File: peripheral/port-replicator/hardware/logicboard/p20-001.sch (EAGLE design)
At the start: 27 parts, among them IC1 74ALS04N, J0 DC9V, J11 AUDIO_JACK_3.5MM_PTH, J12 AUDIO_JACK_3.5MM_PTH, J13 AUDIO_JACK_3.5MM_PTH, J14 AUDIO_JACK_3.5MM_PTH, J7 DIN5, J8 DIN5, J9 DIN5, X0 MKDSN1,5/2-5,08

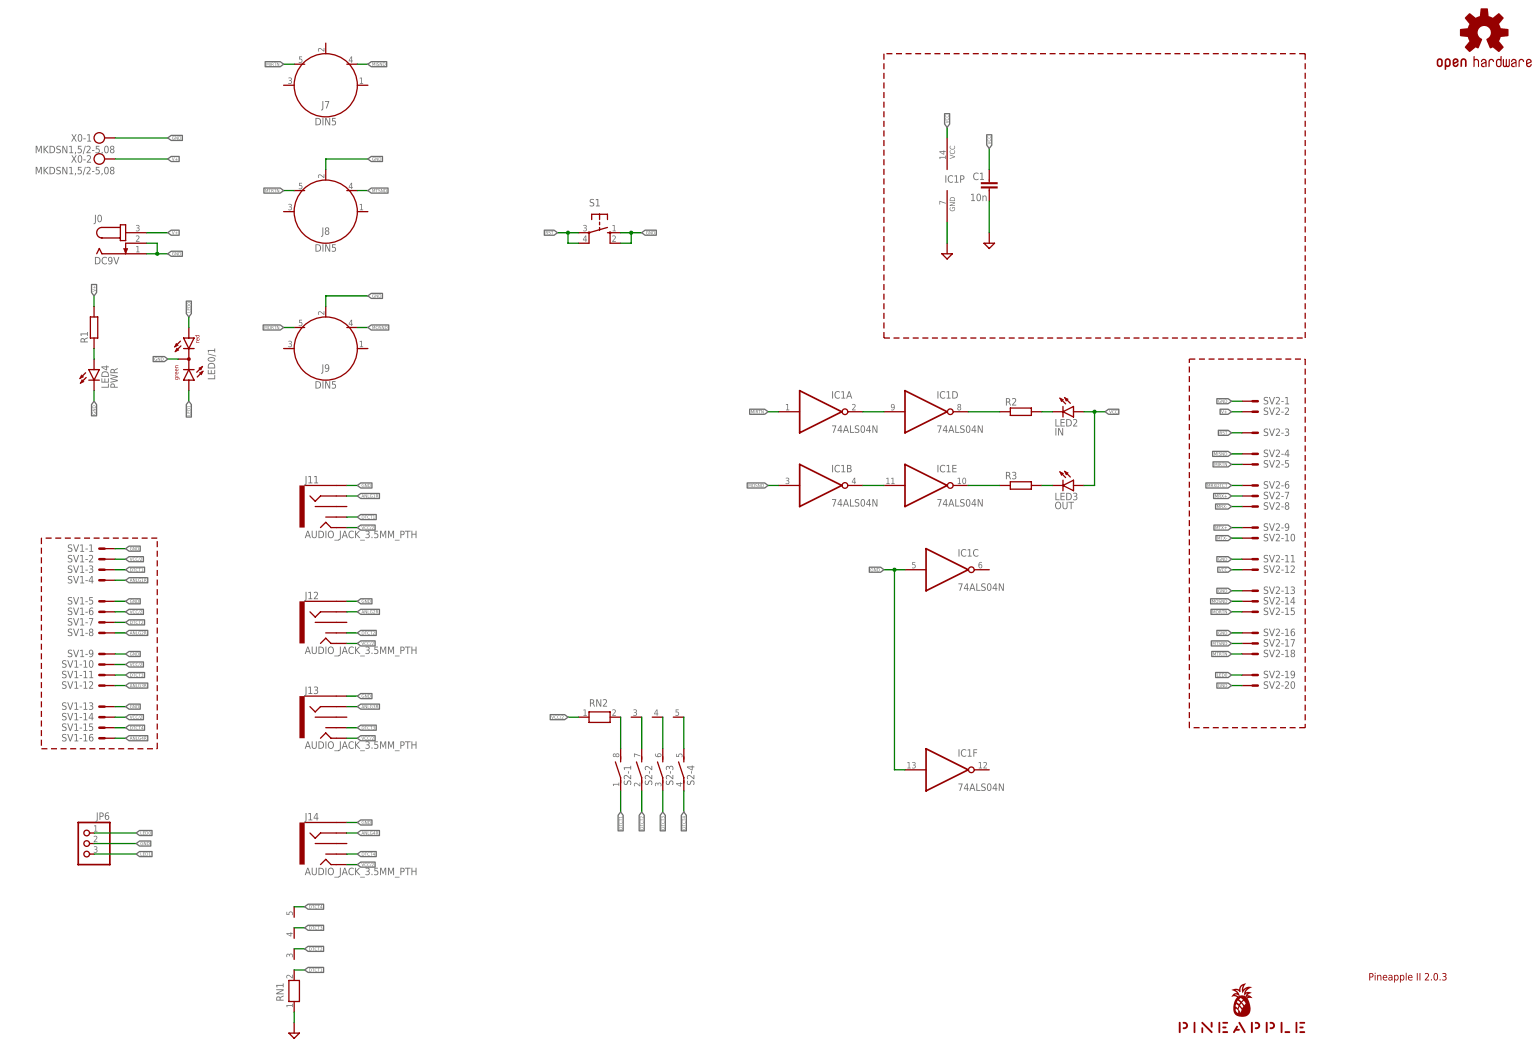
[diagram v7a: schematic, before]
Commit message: Renumbered parts of Pineapple II and port rep.
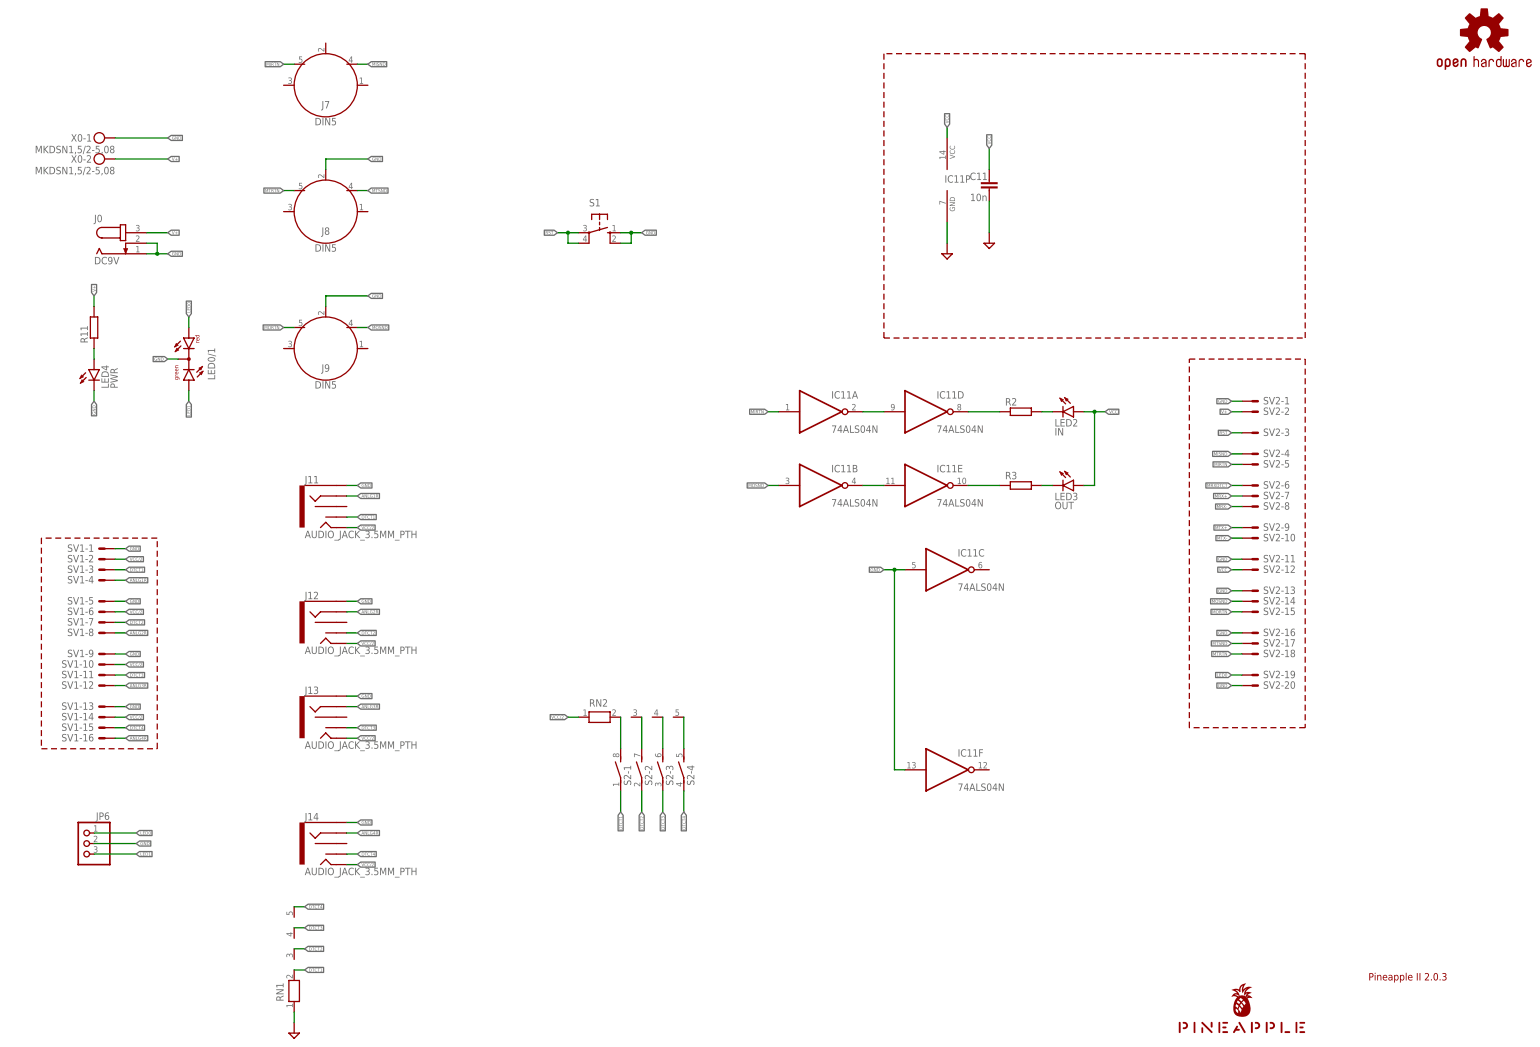
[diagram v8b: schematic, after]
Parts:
- renumbered C1 to C11, IC1 to IC11, R1 to R11
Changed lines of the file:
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@@
 <part name="SV2" library="con-ml" library_urn="urn:adsk.eagle:library:164" deviceset="ML20LE" device="" package3d_urn="urn:adsk.eagle:package:8685/1"/>
 <part name="SUPPLY26" library="supply2" deviceset="GND" device=""/>
-<part name="C1" library="resistor" library_urn="urn:adsk.eagle:library:348" deviceset="C-EU" device="025-024X044" package3d_urn="urn:adsk.eagle:package:23630/1" value="10n"/>
+<part name="C11" library="resistor" library_urn="urn:adsk.eagle:library:348" deviceset="C-EU" device="025-024X044" package3d_urn="urn:adsk.eagle:package:23630/1" value="10n"/>
 <part name="SV1" library="con-ml" library_urn="urn:adsk.eagle:library:164" deviceset="ML16LE" device="" package3d_urn="urn:adsk.eagle:package:8682/1"/>
 <part name="J7" library="SparkFun-Connectors" library_urn="urn:adsk.eagle:library:513" deviceset="DIN5" device="" package3d_urn="urn:adsk.eagle:package:38294/1"/>
@@
 <part name="J13" library="SparkFun-Connectors" library_urn="urn:adsk.eagle:library:513" deviceset="AUDIO_JACK_3.5MM" device="_PTH" package3d_urn="urn:adsk.eagle:package:37997/1"/>
 <part name="J14" library="SparkFun-Connectors" library_urn="urn:adsk.eagle:library:513" deviceset="AUDIO_JACK_3.5MM" device="_PTH" package3d_urn="urn:adsk.eagle:package:37997/1"/>
-<part name="IC1" library="74xx-us" library_urn="urn:adsk.eagle:library:88" deviceset="74*04" device="N" package3d_urn="urn:adsk.eagle:package:16407/2" technology="ALS" value="74ALS04N"/>
-<part name="R1" library="rcl" library_urn="urn:adsk.eagle:library:334" deviceset="R-EU_" device="0204/5" package3d_urn="urn:adsk.eagle:package:23488/1"/>
+<part name="IC11" library="74xx-us" library_urn="urn:adsk.eagle:library:88" deviceset="74*04" device="N" package3d_urn="urn:adsk.eagle:package:16407/2" technology="ALS" value="74ALS04N"/>
+<part name="R11" library="rcl" library_urn="urn:adsk.eagle:library:334" deviceset="R-EU_" device="0204/5" package3d_urn="urn:adsk.eagle:package:23488/1"/>
 <part name="R2" library="rcl" library_urn="urn:adsk.eagle:library:334" deviceset="R-EU_" device="0204/5" package3d_urn="urn:adsk.eagle:package:23488/1"/>
 <part name="LED4" library="led" library_urn="urn:adsk.eagle:library:259" deviceset="LED" device="3MM" package3d_urn="urn:adsk.eagle:package:15797/1" value="PWR"/>
@@
 </instance>
 <instance part="SUPPLY26" gate="GND" x="251.46" y="198.12" smashed="yes"/>
-<instance part="C1" gate="G$1" x="251.46" y="213.36" smashed="yes">
+<instance part="C11" gate="G$1" x="251.46" y="213.36" smashed="yes">
 <attribute name="NAME" x="248.92" y="213.36" size="1.778" layer="95" align="bottom-center"/>
 <attribute name="VALUE" x="248.92" y="208.28" size="1.778" layer="96" align="bottom-center"/>
@@
 <attribute name="VALUE" x="86.36" y="45.72" size="1.778" layer="96" font="vector"/>
 </instance>
-<instance part="IC1" gate="A" x="210.82" y="157.48" smashed="yes">
+<instance part="IC11" gate="A" x="210.82" y="157.48" smashed="yes">
 <attribute name="NAME" x="213.36" y="160.655" size="1.778" layer="95"/>
 <attribute name="VALUE" x="213.36" y="152.4" size="1.778" layer="96"/>
 </instance>
-<instance part="IC1" gate="B" x="210.82" y="139.7" smashed="yes">
+<instance part="IC11" gate="B" x="210.82" y="139.7" smashed="yes">
 <attribute name="NAME" x="213.36" y="142.875" size="1.778" layer="95"/>
 <attribute name="VALUE" x="213.36" y="134.62" size="1.778" layer="96"/>
 </instance>
-<instance part="IC1" gate="C" x="241.3" y="119.38" smashed="yes">
+<instance part="IC11" gate="C" x="241.3" y="119.38" smashed="yes">
 <attribute name="NAME" x="243.84" y="122.555" size="1.778" layer="95"/>
 <attribute name="VALUE" x="243.84" y="114.3" size="1.778" layer="96"/>
 </instance>
-<instance part="IC1" gate="D" x="236.22" y="157.48" smashed="yes">
+<instance part="IC11" gate="D" x="236.22" y="157.48" smashed="yes">
 <attribute name="NAME" x="238.76" y="160.655" size="1.778" layer="95"/>
 <attribute name="VALUE" x="238.76" y="152.4" size="1.778" layer="96"/>
 </instance>
-<instance part="IC1" gate="E" x="236.22" y="139.7" smashed="yes">
+<instance part="IC11" gate="E" x="236.22" y="139.7" smashed="yes">
 <attribute name="NAME" x="238.76" y="142.875" size="1.778" layer="95"/>
 <attribute name="VALUE" x="238.76" y="134.62" size="1.778" layer="96"/>
 </instance>
-<instance part="IC1" gate="F" x="241.3" y="71.12" smashed="yes">
+<instance part="IC11" gate="F" x="241.3" y="71.12" smashed="yes">
 <attribute name="NAME" x="243.84" y="74.295" size="1.778" layer="95"/>
 <attribute name="VALUE" x="243.84" y="66.04" size="1.778" layer="96"/>
 </instance>
-<instance part="R1" gate="G$1" x="35.56" y="177.8" smashed="yes" rot="R90">
+<instance part="R11" gate="G$1" x="35.56" y="177.8" smashed="yes" rot="R90">
 <attribute name="NAME" x="34.0614" y="173.99" size="1.778" layer="95" rot="R90"/>
 <attribute name="VALUE" x="38.862" y="173.99" size="1.778" layer="96" rot="R90"/>
@@
 <attribute name="VALUE" x="255.27" y="136.398" size="1.778" layer="96"/>
 </instance>
-<instance part="IC1" gate="P" x="241.3" y="213.36" smashed="yes">
+<instance part="IC11" gate="P" x="241.3" y="213.36" smashed="yes">
 <attribute name="NAME" x="240.665" y="212.725" size="1.778" layer="95"/>
 </instance>
@@
 <pinref part="SUPPLY26" gate="GND" pin="GND"/>
 <wire x1="251.46" y1="208.28" x2="251.46" y2="200.66" width="0.1524" layer="91"/>
-<pinref part="C1" gate="G$1" pin="2"/>
+<pinref part="C11" gate="G$1" pin="2"/>
 </segment>
 <segment>
@@
 </segment>
 <segment>
-<pinref part="IC1" gate="F" pin="I"/>
+<pinref part="IC11" gate="F" pin="I"/>
 <wire x1="231.14" y1="71.12" x2="228.6" y2="71.12" width="0.1524" layer="91"/>
-<pinref part="IC1" gate="C" pin="I"/>
+<pinref part="IC11" gate="C" pin="I"/>
 <wire x1="231.14" y1="119.38" x2="228.6" y2="119.38" width="0.1524" layer="91"/>
 <wire x1="228.6" y1="71.12" x2="228.6" y2="119.38" width="0.1524" layer="91"/>
@@
 </segment>
 <segment>
-<pinref part="IC1" gate="P" pin="GND"/>
+<pinref part="IC11" gate="P" pin="GND"/>
 <wire x1="241.3" y1="203.2" x2="241.3" y2="198.12" width="0.1524" layer="91"/>
 <pinref part="SUPPLY1" gate="GND" pin="GND"/>
@@
 <segment>
 <wire x1="251.46" y1="220.98" x2="251.46" y2="215.9" width="0.1524" layer="91"/>
-<pinref part="C1" gate="G$1" pin="1"/>
+<pinref part="C11" gate="G$1" pin="1"/>
 <label x="251.46" y="220.98" size="0.8128" layer="95" rot="R90" xref="yes"/>
 </segment>
@@
 </segment>
 <segment>
-<pinref part="IC1" gate="P" pin="VCC"/>
+<pinref part="IC11" gate="P" pin="VCC"/>
 <wire x1="241.3" y1="223.52" x2="241.3" y2="226.06" width="0.1524" layer="91"/>
 <label x="241.3" y="226.06" size="0.8128" layer="95" rot="R90" xref="yes"/>
@@
 </segment>
 <segment>
-<pinref part="IC1" gate="A" pin="I"/>
+<pinref part="IC11" gate="A" pin="I"/>
 <wire x1="200.66" y1="157.48" x2="198.12" y2="157.48" width="0.1524" layer="91"/>
 <label x="198.12" y="157.48" size="0.8128" layer="95" rot="R180" xref="yes"/>
@@
 </segment>
 <segment>
-<pinref part="IC1" gate="B" pin="I"/>
+<pinref part="IC11" gate="B" pin="I"/>
 <wire x1="200.66" y1="139.7" x2="198.12" y2="139.7" width="0.1524" layer="91"/>
 <label x="198.12" y="139.7" size="0.8128" layer="95" rot="R180" xref="yes"/>
@@
 </segment>
 <segment>
-<pinref part="R1" gate="G$1" pin="2"/>
+<pinref part="R11" gate="G$1" pin="2"/>
 <wire x1="35.56" y1="185.42" x2="35.56" y2="182.88" width="0.1524" layer="91"/>
 <label x="35.56" y="185.42" size="0.8128" layer="95" rot="R90" xref="yes"/>
@@
 <net name="LEDPWR" class="0">
 <segment>
-<pinref part="R1" gate="G$1" pin="1"/>
+<pinref part="R11" gate="G$1" pin="1"/>
 <pinref part="LED4" gate="G$1" pin="A"/>
 <wire x1="35.56" y1="172.72" x2="35.56" y2="170.18" width="0.1524" layer="91"/>
@@
 <net name="N$1" class="0">
 <segment>
-<pinref part="IC1" gate="A" pin="O"/>
-<pinref part="IC1" gate="D" pin="I"/>
+<pinref part="IC11" gate="A" pin="O"/>
+<pinref part="IC11" gate="D" pin="I"/>
 <wire x1="220.98" y1="157.48" x2="226.06" y2="157.48" width="0.1524" layer="91"/>
 </segment>
@@
 <net name="N$2" class="0">
 <segment>
-<pinref part="IC1" gate="B" pin="O"/>
-<pinref part="IC1" gate="E" pin="I"/>
+<pinref part="IC11" gate="B" pin="O"/>
+<pinref part="IC11" gate="E" pin="I"/>
 <wire x1="220.98" y1="139.7" x2="226.06" y2="139.7" width="0.1524" layer="91"/>
 </segment>
@@
 <net name="N$3" class="0">
 <segment>
-<pinref part="IC1" gate="D" pin="O"/>
+<pinref part="IC11" gate="D" pin="O"/>
 <pinref part="R2" gate="G$1" pin="1"/>
 <wire x1="246.38" y1="157.48" x2="254" y2="157.48" width="0.1524" layer="91"/>
@@
 <net name="N$4" class="0">
 <segment>
-<pinref part="IC1" gate="E" pin="O"/>
+<pinref part="IC11" gate="E" pin="O"/>
 <pinref part="R3" gate="G$1" pin="1"/>
 <wire x1="246.38" y1="139.7" x2="254" y2="139.7" width="0.1524" layer="91"/>
